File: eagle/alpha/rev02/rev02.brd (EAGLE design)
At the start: 100 x 80 mm, 322 parts, among them CN1 HOST, IC1 IS45S32160F, IC3 N25Q128A13ES, Q3 2N7002, Q5 ASFL1, Q6 2N7002, T1 BC847, T2 BC847, T3 BC818, U1 MC14551BDG, U2 MC74HC1G14DTT1G, U3 ATTINY828R-AU, U4 MC14551BDG, U5 23K640-I/SN, U6 MCP79412-I/SN, U7 XC7A200TFBG484, Y1 12 MHz

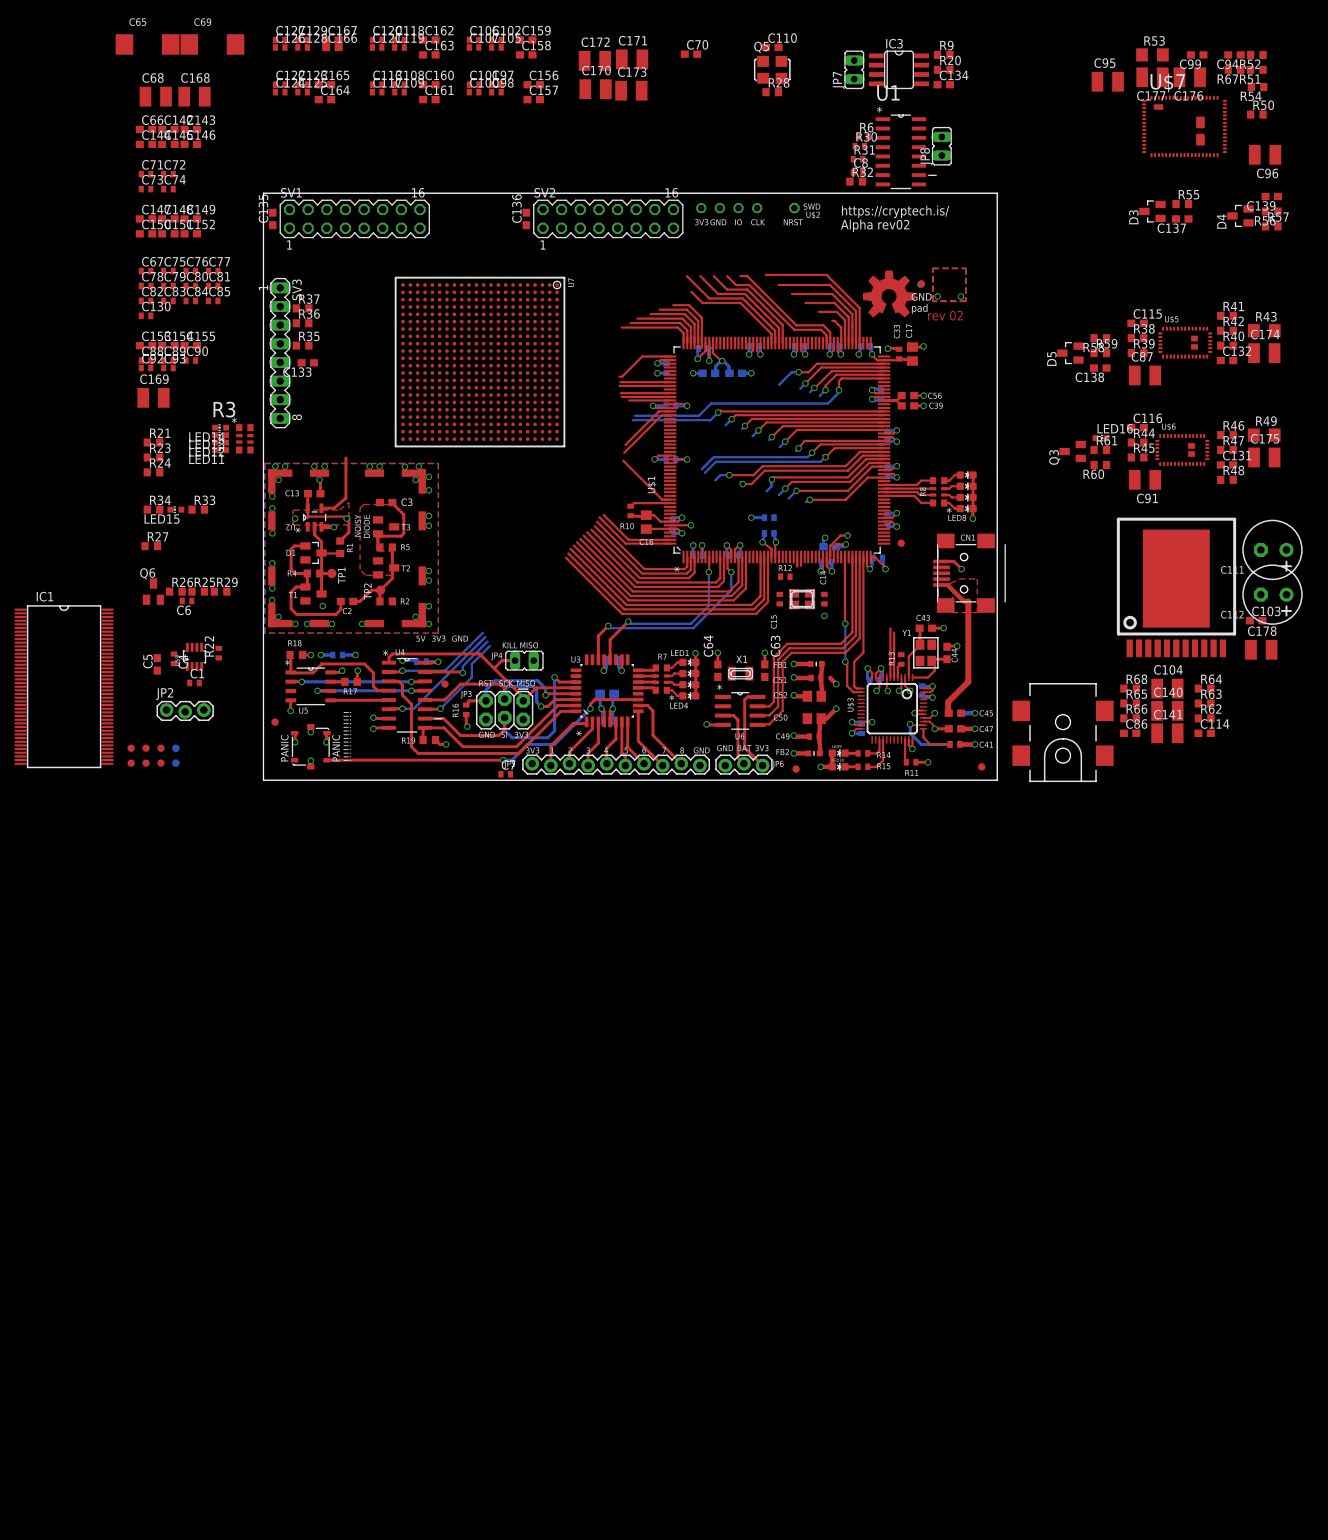
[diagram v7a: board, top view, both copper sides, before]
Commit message: connect first SDRAM, add USB MGMT UART.
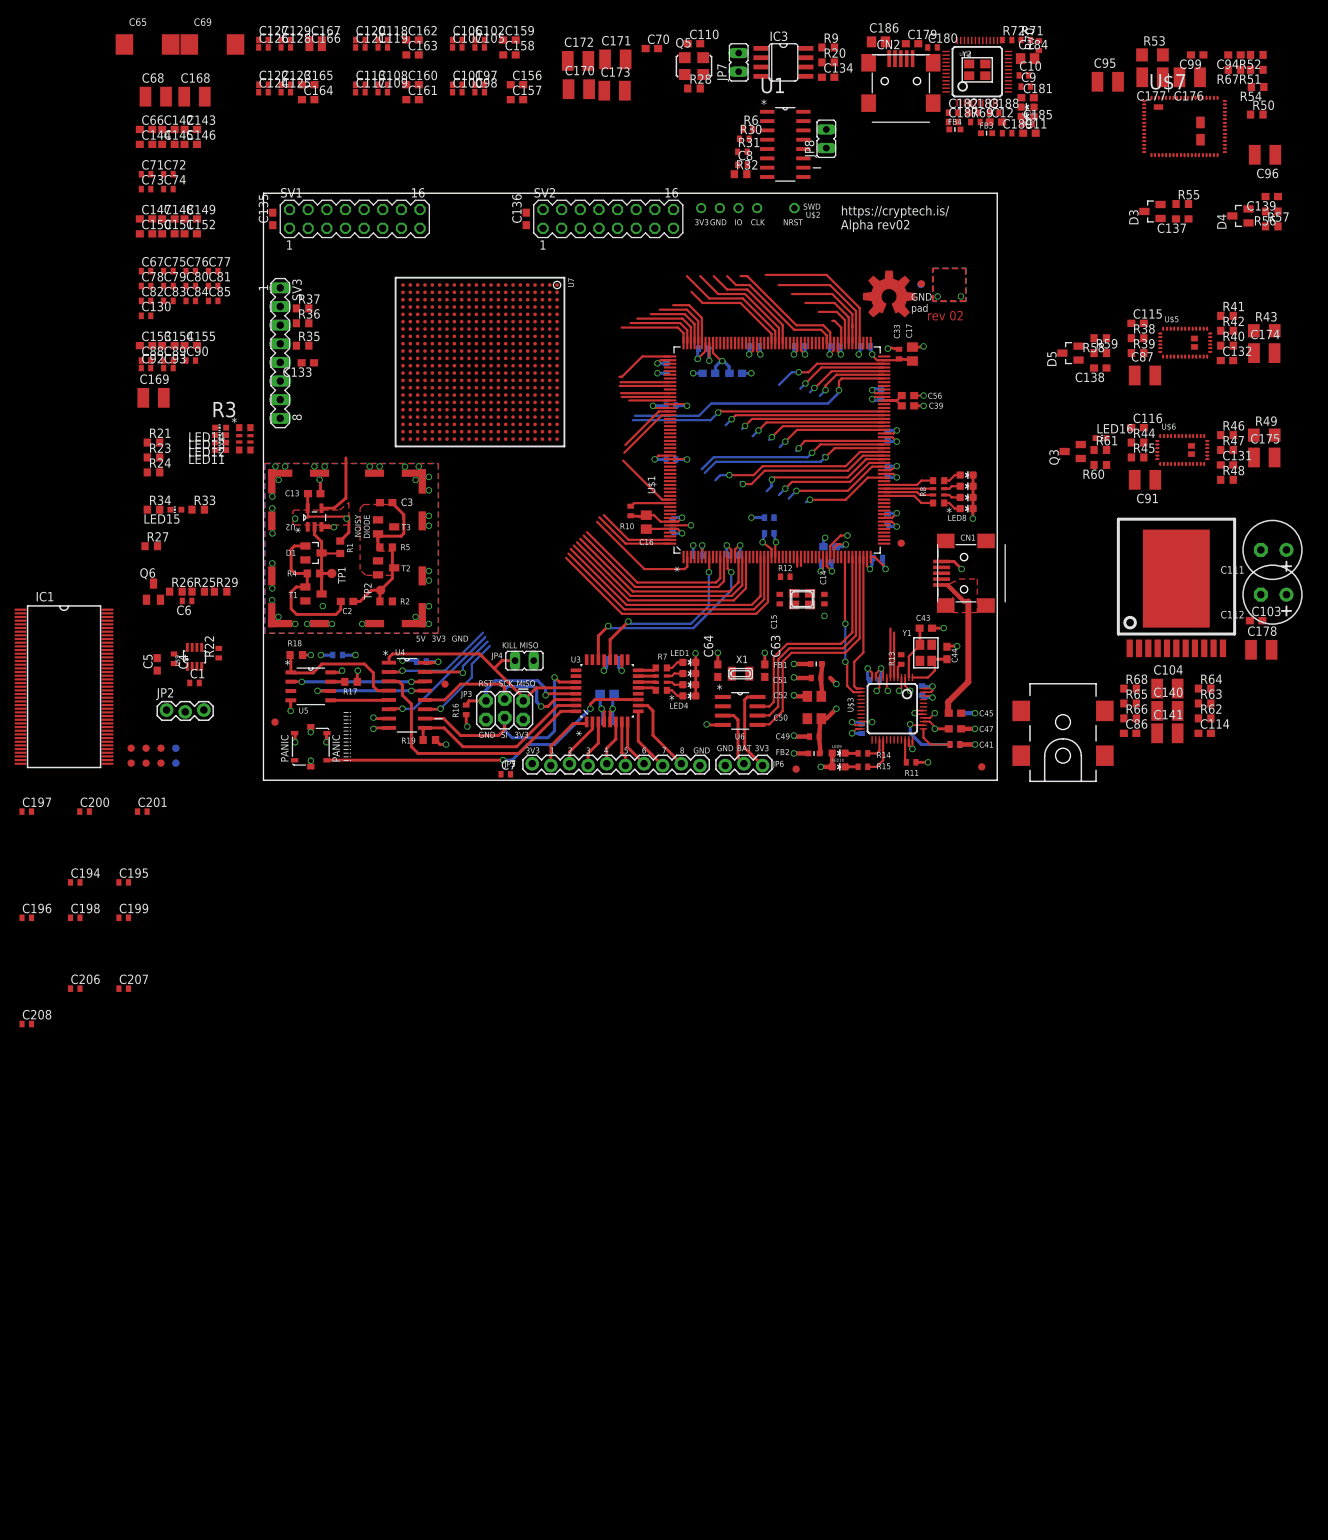
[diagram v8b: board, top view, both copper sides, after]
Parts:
- added C10, C180, C182, C183, C185, C187, C188, C189, C197, C200, C201, C9: 0.1 uF, resistor:C0402
- added C11, C12: 5 pF, rcl:C0603
- added C179, C181: 4.7 uF, resistor:C0603
- added C184, C186: 10 uF, resistor:C0805
- added C194, C195, C196, C198, C199, C206, C207, C208: 0.1uF, resistor:C0402
- added CN2: HOST, adafruit:USB-MINIB
- added FB3, FB4: 600R 500mA, microbuilder:_0603MP
- added LED17: YELLOW, SparkFun-LED:LED-0603
- added LED18: GREEN, SparkFun-LED:LED-0603
- added R69: 10K, resistor:R0402
- added R70: 12K, resistor:R0402
- added R71, R72: 220, resistor:R0402
- added U$10: FT232H_SERIAL, FT232H:FT2323HL_LQFP48
- added Y2: 12 MHz, microbuilder:CRYSTAL_3.2X2.5
- moved C8 15.8 mm to (85.3, 84.6)
- moved IC3 15.8 mm to (90.9, 98.6)
- moved JP7 15.8 mm to (84.8, 98.6)
- moved JP8 15.8 mm to (96.8, 88.1)
- moved R30 15.8 mm to (85.6, 88.1)
- moved R31 15.8 mm to (85.3, 86.4)
- moved R6 15.8 mm to (86.1, 89.4)
- moved C134 15.8 mm to (97.0, 96.5)
- moved R20 15.8 mm to (97.0, 98.6)
- moved R32 15.8 mm to (85.1, 83.3)
- moved R9 15.8 mm to (97.0, 100.6)
- moved U1 15.8 mm to (91.2, 87.4)
- moved C110 10.7 mm to (78.7, 101.1)
- moved Q5 10.7 mm to (78.7, 98.0)
- moved R28 10.7 mm to (78.7, 95.0)
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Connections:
- removed net FPGA_FMC_CLK: U$1.167, U7.W11
- removed net VSS: IC1.44, IC1.58, IC1.72, IC1.86
- removed net VSSQ: IC1.12, IC1.32, IC1.38, IC1.46, IC1.52, IC1.6, IC1.78, IC1.84
- new net FMC_CLK: IC1.68, U$1.167, U7.W11
- new net FMC_NBL0: IC1.16, U$1.200
- new net FMC_NBL1: IC1.71, U$1.201
- new net FMC_NBL2: IC1.28, U$1.205
- new net FMC_NBL3: IC1.59, U$1.206
- new net FMC_SDCKE0: IC1.67, U$1.38
- new net FMC_SDNCAS: IC1.18, U$1.191
- new net FMC_SDNE0: IC1.20, U$1.37
- new net FMC_SDNRAS: IC1.19, U$1.70
- new net FMC_SDNWE: IC1.17, U$1.35
- new net FT_MGMT_CTS: U$10.16
- new net FT_MGMT_DTR: U$10.17
- new net FT_MGMT_RTS: U$10.15
- new net FT_MGMT_RXD: U$10.14
- new net FT_MGMT_TXD: U$10.13
- new net FT_MGMT_VCC3V3: C181.1, C182.1, C187.1, C188.1, C189.1, FB3.1, FB4.1, LED17.A, LED18.A, R69.2, U$10.12, U$10.24, U$10.39, U$10.46
- new net FT_MGMT_VPHY: U$10.3
- new net FT_MGMT_VPLL: C185.1, C186.1, FB3.2, U$10.8
- new net FT_MGMT_VREGIN: C179.1, C180.1, CN2.VBUS, U$10.40
- new net FT_REF1: R70.1, U$10.5
- new net FT_RESET1: R69.1, U$10.34
- new net FT_RXLED1: R71.2, U$10.27
- new net FT_TXLED1: R72.2, U$10.28
- new net FT_VCCA1: C9.1, U$10.37
- new net FT_VCCORE1: C10.1, U$10.38
- new net N$6: LED17.C, R71.1
- new net N$7: LED18.C, R72.1
- new net N$8: C11.2, U$10.2, Y2.2
- new net N$9: C12.2, U$10.1, Y2.1
- new net USB_MGMT_DM: CN2.D-, U$10.6
- new net USB_MGMT_DP: CN2.D+, U$10.7
- net FMC_A0: now also IC1.25
- net FMC_A1: now also IC1.26
- net FMC_A10: now also IC1.24
- net FMC_A11: now also IC1.21
- net FMC_A12: now also IC1.69
- net FMC_A14: now also IC1.22
- net FMC_A15: now also IC1.23
- net FMC_A2: now also IC1.27
- net FMC_A22: now also U$1.5
- net FMC_A23: now also U$1.1
- net FMC_A24: now also U$1.182
- net FMC_A25: now also U$1.183
- net FMC_A3: now also IC1.60
- net FMC_A4: now also IC1.61
- net FMC_A5: now also IC1.62
- net FMC_A6: now also IC1.63
- net FMC_A7: now also IC1.64
- net FMC_A8: now also IC1.65
- net FMC_A9: now also IC1.66
- net FMC_D10: now also IC1.76
- net FMC_D18: no longer IC1.36
- net FMC_D19: now also IC1.36
- net FMC_D9: no longer IC1.76
- net FT_VPHY: now also C183.1, C184.1, FB4.2
- net GND: now also C10.2, C11.1, C12.1, C179.2, C180.2, C181.2, C182.2, C183.2, C184.2, C185.2, C186.2, C187.2, C188.2, C189.2, C194.2, C195.2, C196.2, C197.2, C198.2, C199.2, C200.2, C201.2, C206.2, C207.2, C208.2, C9.2, CN2.GND, IC1.12, IC1.32, IC1.38, IC1.44, IC1.46, IC1.52, IC1.58, IC1.6, IC1.72, IC1.78, IC1.84, IC1.86, R70.2, U$10.10, U$10.11, U$10.22, U$10.23, U$10.35, U$10.36, U$10.4, U$10.41, U$10.42, U$10.47, U$10.48, U$10.9
- net VCCO_3V3: now also C194.1, C195.1, C196.1, C197.1, C198.1, C199.1, C200.1, C201.1, C206.1, C207.1, C208.1, IC1.15, IC1.29, IC1.35, IC1.41, IC1.43, IC1.49, IC1.55, IC1.75, IC1.81
- net VDD: no longer IC1.15, IC1.29, IC1.43
- net VDDQ: no longer IC1.35, IC1.41, IC1.49, IC1.55, IC1.75, IC1.81
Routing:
- net FMC_A21: track 19.2 -> 0.00 mm
- net FMC_A20: track 17.7 -> 0.00 mm
- net FPGA_FMC_CLK: track 6.71 -> 0.00 mm
- net FMC_CLK: track 0.00 -> 6.71 mm
